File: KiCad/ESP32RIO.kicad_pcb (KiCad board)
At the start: 2 copper layers, 39 parts, among them J1 Screw_Terminal_01x08, J2 Screw_Terminal_01x08, J3 Screw_Terminal_01x08, J4 Screw_Terminal_01x08, U1 PC817, U10 PC817, U11 PC817, U12 PC817, U13 PC817, U14 PC817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

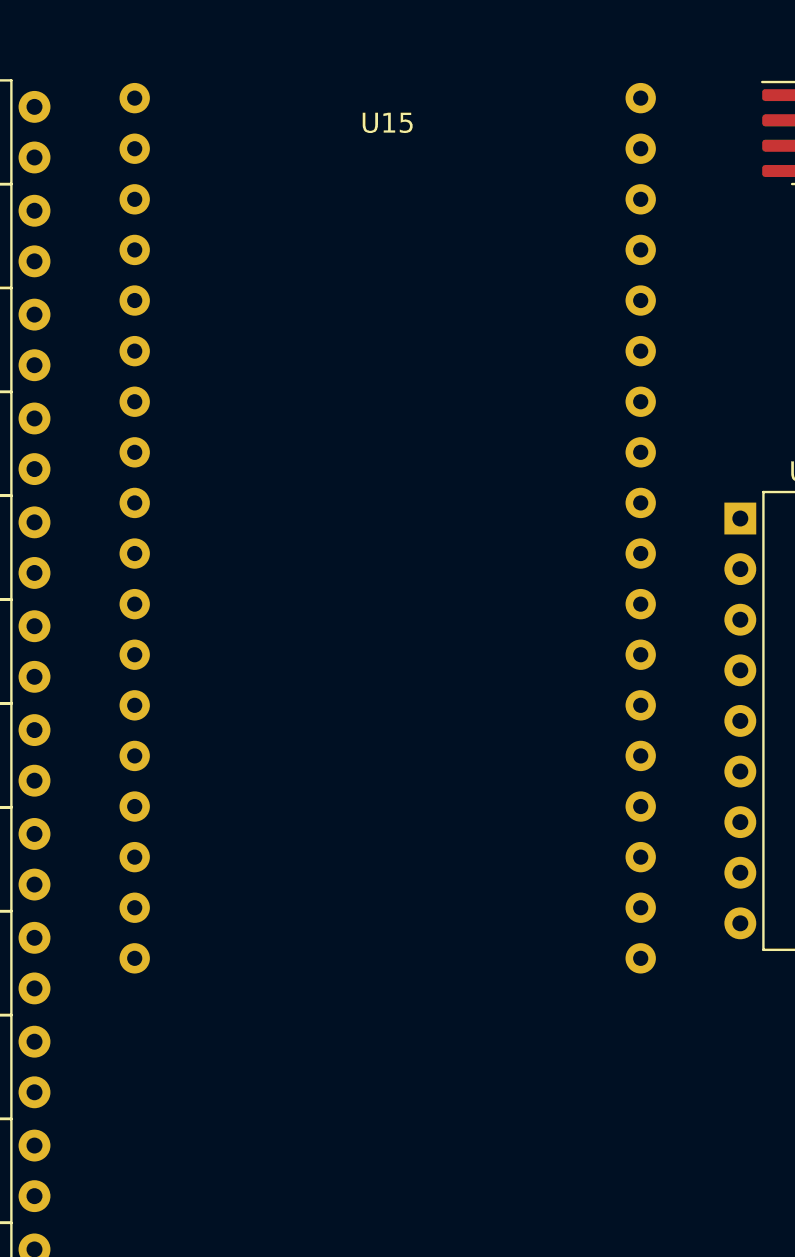
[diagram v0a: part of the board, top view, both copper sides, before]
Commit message: 14DI og 2 AI virker
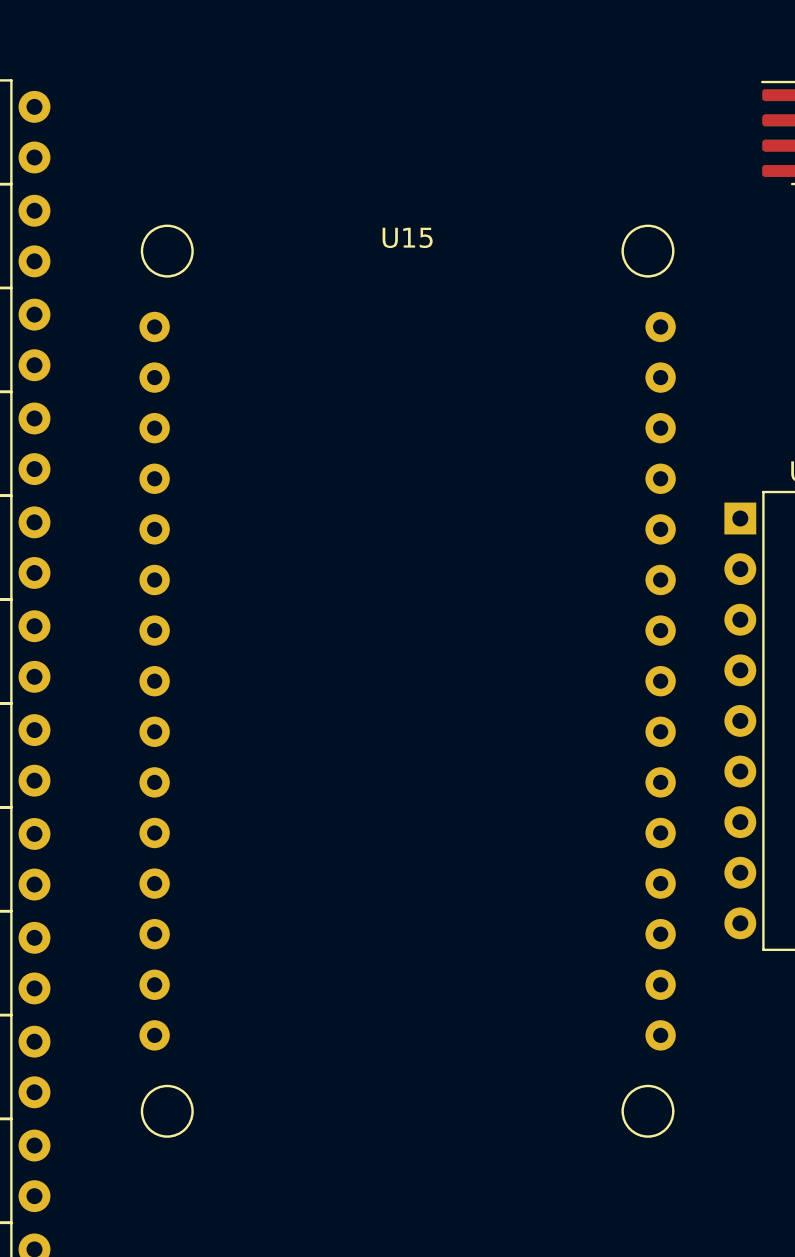
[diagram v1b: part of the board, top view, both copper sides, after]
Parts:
- U15: value DOIT-ESP32-DEVKIT-V1 -> ESP32-DEVKIT-V1
- moved U15 7.11 mm to (173.8, 41.0)
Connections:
- U1 pad 3: Net-(U1-Pad3) -> unconnected-(U1-Pad3)
- U15 pad 17: GND -> unconnected-(U15-Pad17)
- U15 pad 19: Net-(U15-Pad19) -> unconnected-(U15-Pad19)
- U15 pad 2: Net-(U1-Pad3) -> Net-(U15-Pad2)
- U15 pad 29: unconnected-(U15-Pad29) -> Net-(U15-Pad2)
- U15 pad 8: Net-(U15-Pad8) -> unconnected-(U15-Pad8)
- U16 pad 8: Net-(U15-Pad19) -> Net-(C1-Pad1)
- U4 pad 3: Net-(U15-Pad8) -> unconnected-(U4-Pad3)
